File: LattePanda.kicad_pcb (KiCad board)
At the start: 2 copper layers, 70 x 88 mm, 18 parts, among them IC1 NJM2845MABDT

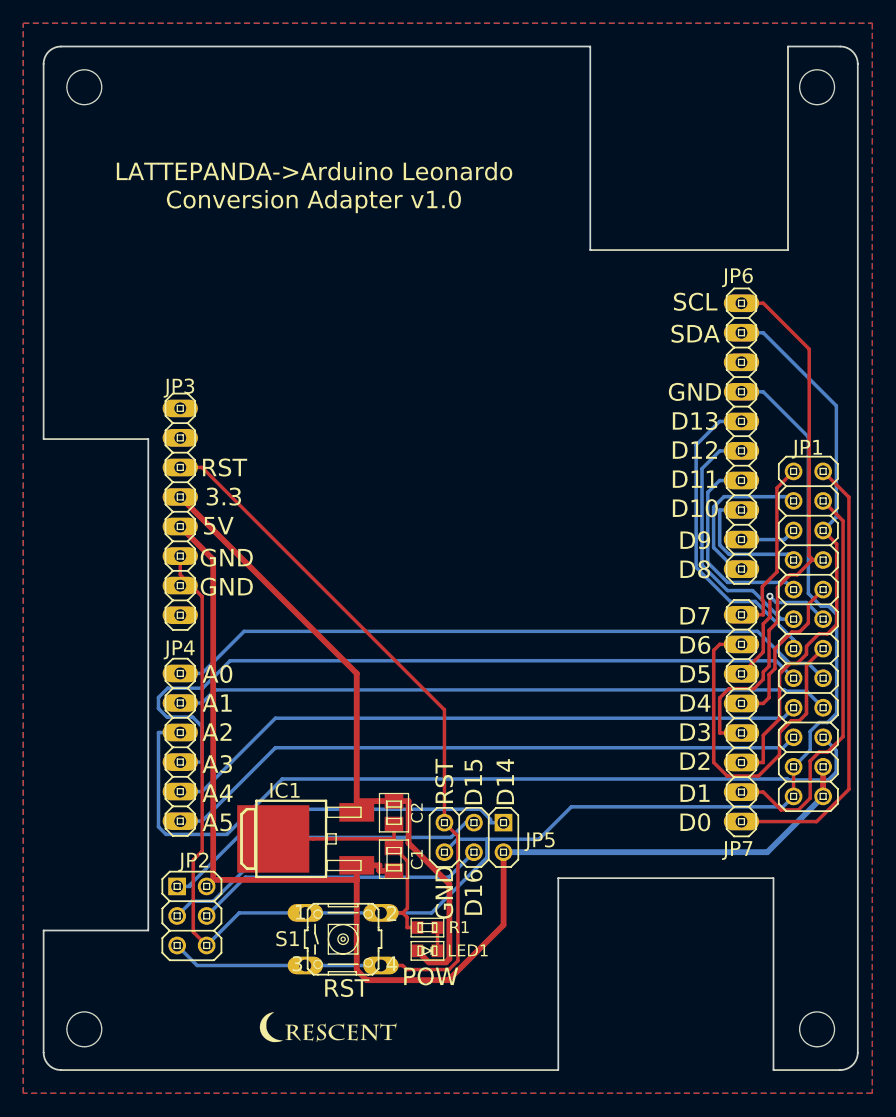
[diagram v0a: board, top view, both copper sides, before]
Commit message: Fixed the interference of LAN port.
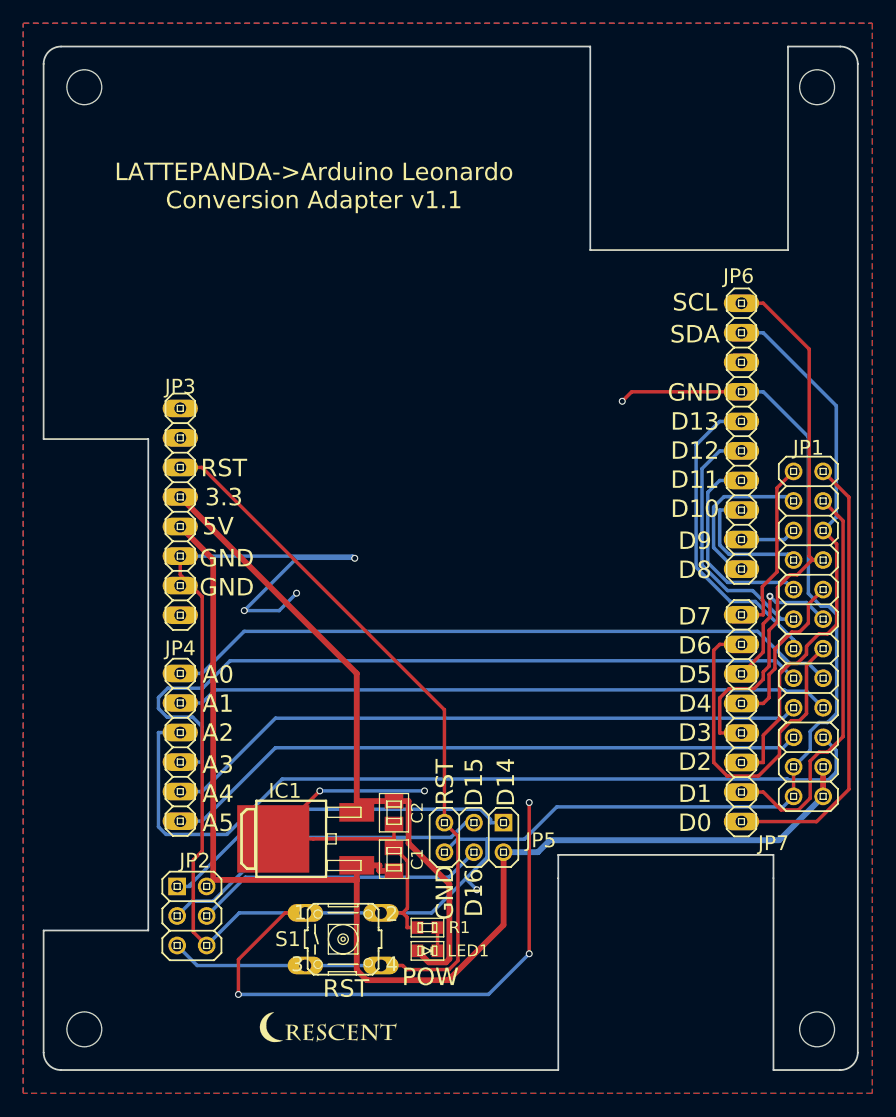
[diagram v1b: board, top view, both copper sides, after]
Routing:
- net GND: track 161.2 -> 269.3 mm, vias 0 -> 10
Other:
- outline, holes or cut-outs redrawn
- board text added: "LATTEPANDA->Arduino Leonardo Conversion Adapter v1.1"
- board text removed: "LATTEPANDA->Arduino Leonardo Conversion Adapter v1.0"
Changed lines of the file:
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@@
     (area 88.750001 44.65 181.740046 140.47626)
     (thickness 1.6)
-    (drawings 58)
-    (tracks 267)
+    (drawings 60)
+    (tracks 298)
     (zones 0)
     (modules 18)
@@
   (title_block
     (title "LattePanda to Arduino Leonard")
-    (date 2017-06-17)
-    (rev v1.0)
+    (date 2017-07-07)
+    (rev v1.1)
     (company Crescent)
   )
@@
     (tags "PIN HEADER")
     (attr virtual)
-    (fp_text reference JP7 (at -11.25 -0.25 180) (layer F.SilkS)
+    (fp_text reference JP7 (at -10.75 2.75 180) (layer F.SilkS)
       (effects (font (size 1.27 1.27) (thickness 0.127)))
     )
@@
       (net 2 GND))
   )
+  (gr_line (start 151 119.5) (end 151 121.5) (angle 90) (layer Edge.Cuts) (width 0.15))
+  (gr_line (start 169.5 119.5) (end 151 119.5) (angle 90) (layer Edge.Cuts) (width 0.15))
+  (gr_line (start 169.5 121.5) (end 169.5 119.5) (angle 90) (layer Edge.Cuts) (width 0.15))
   (gr_text POW (at 140 130) (layer F.SilkS)
     (effects (font (size 1.5 1.5) (thickness 0.3)))
@@
     (effects (font (size 1.5 1.5) (thickness 0.3)))
   )
-  (gr_text "LATTEPANDA->Arduino Leonardo\nConversion Adapter v1.0" (at 130 62) (layer F.SilkS)
+  (gr_text "LATTEPANDA->Arduino Leonardo\nConversion Adapter v1.1" (at 130 62) (layer F.SilkS)
     (effects (font (size 1.5 1.5) (thickness 0.3)))
   )
@@
   (gr_line (start 169.5 138) (end 175.25 138) (angle 90) (layer Edge.Cuts) (width 0.15))
   (gr_line (start 169.5 121.5) (end 169.5 138) (angle 90) (layer Edge.Cuts) (width 0.15))
-  (gr_line (start 151 121.5) (end 169.5 121.5) (angle 90) (layer Edge.Cuts) (width 0.15))
   (gr_line (start 151 138) (end 151 121.5) (angle 90) (layer Edge.Cuts) (width 0.15))
   (gr_line (start 108.25 138) (end 151 138) (angle 90) (layer Edge.Cuts) (width 0.15))
@@
     (arrow2b (pts (xy 110.25 47.5) (xy 111.376504 46.913579)))
   )
+  (segment (start 170 118.24) (end 150.28 118.24) (width 0.5) (layer B.Cu) (net 1))
+  (segment (start 173.77 114.47) (end 170 118.24) (width 0.5) (layer B.Cu) (net 1))
+  (segment (start 149.25 119.27) (end 146.29 119.27) (width 0.5) (layer B.Cu) (net 1))
+  (segment (start 150.28 118.24) (end 149.25 119.27) (width 0.5) (layer B.Cu) (net 1))
   (segment (start 135.6233 120.8706) (end 135.6259 120.8732) (width 0.5) (layer F.Cu) (net 1))
   (segment (start 135.6233 120.4034) (end 135.6233 120.8706) (width 0.5) (layer F.Cu) (net 1))
@@
   (segment (start 121.3275 121.6525) (end 120.77 122.21) (width 0.5) (layer F.Cu) (net 1))
   (segment (start 173.77 114.47) (end 173.77 111.93) (width 0.5) (layer F.Cu) (net 1))
-  (segment (start 168.97 119.27) (end 146.29 119.27) (width 0.5) (layer B.Cu) (net 1))
-  (segment (start 173.77 114.47) (end 168.97 119.27) (width 0.5) (layer B.Cu) (net 1))
   (segment (start 133.6731 121.6525) (end 121.3275 121.6525) (width 0.5) (layer F.Cu) (net 1))
   (segment (start 146.29 125.5301) (end 146.29 119.27) (width 0.5) (layer F.Cu) (net 1))
@@
   (segment (start 133.6731 129.4095) (end 134.5343 130.2707) (width 0.5) (layer F.Cu) (net 1))
   (segment (start 133.6731 121.6525) (end 133.6731 129.4095) (width 0.5) (layer F.Cu) (net 1))
+  (segment (start 148.5 115) (end 148.5 128) (width 0.3) (layer F.Cu) (net 2))
+  (segment (start 145 131.5) (end 148.5 128) (width 0.3) (layer B.Cu) (net 2))
+  (via (at 148.5 128) (size 0.6) (drill 0.4) (layers F.Cu B.Cu) (net 2))
+  (segment (start 127.5106 124.4894) (end 129.2488 124.4894) (width 0.3) (layer F.Cu) (net 2))
+  (via (at 123.5 131.5) (size 0.6) (drill 0.4) (layers F.Cu B.Cu) (net 2))
+  (segment (start 123.5 128.5) (end 123.5 131.5) (width 0.3) (layer F.Cu) (net 2))
+  (segment (start 127.5106 124.4894) (end 123.5 128.5) (width 0.3) (layer F.Cu) (net 2))
+  (segment (start 123.5 131.5) (end 145 131.5) (width 0.3) (layer B.Cu) (net 2))
+  (via (at 148.5 115) (size 0.6) (drill 0.4) (layers F.Cu B.Cu) (net 2))
+  (segment (start 143.04745 121.54745) (end 144 122.5) (width 0.3) (layer B.Cu) (net 2))
+  (via (at 144 122.5) (size 0.6) (drill 0.4) (layers F.Cu B.Cu) (net 2))
+  (segment (start 124 98.5) (end 127 98.5) (width 0.3) (layer B.Cu) (net 2))
+  (segment (start 128.5 94) (end 124 98.5) (width 0.3) (layer B.Cu) (net 2))
+  (via (at 124 98.5) (size 0.6) (drill 0.4) (layers F.Cu B.Cu) (net 2))
+  (segment (start 118.5 93.81) (end 133.31 93.81) (width 0.3) (layer B.Cu) (net 2))
+  (via (at 133.5 94) (size 0.6) (drill 0.4) (layers F.Cu B.Cu) (net 2))
+  (segment (start 133.31 93.81) (end 133.5 94) (width 0.3) (layer B.Cu) (net 2))
+  (segment (start 133.5 94) (end 128.5 94) (width 0.3) (layer B.Cu) (net 2))
+  (via (at 128.5 97) (size 0.6) (drill 0.4) (layers F.Cu B.Cu) (net 2))
+  (segment (start 127 98.5) (end 128.5 97) (width 0.3) (layer B.Cu) (net 2))
+  (segment (start 139.5 114) (end 130.5 114) (width 0.3) (layer B.Cu) (net 2))
+  (via (at 130.5 114) (size 0.6) (drill 0.4) (layers F.Cu B.Cu) (net 2))
+  (segment (start 130.5 114) (end 126.49502 118.00498) (width 0.3) (layer F.Cu) (net 2))
+  (via (at 139.5 114) (size 0.6) (drill 0.4) (layers F.Cu B.Cu) (net 2))
+  (segment (start 126.49502 118.125) (end 126.49502 118.00498) (width 0.3) (layer F.Cu) (net 2))
+  (segment (start 166.75 79.69) (end 157.31 79.69) (width 0.3) (layer F.Cu) (net 2))
+  (via (at 156.5 80.5) (size 0.6) (drill 0.4) (layers F.Cu B.Cu) (net 2))
+  (segment (start 157.31 79.69) (end 156.5 80.5) (width 0.3) (layer F.Cu) (net 2))
   (segment (start 171.23 114.47) (end 171.23 111.93) (width 0.3) (layer F.Cu) (net 2))
   (segment (start 123.5706 124.4894) (end 120.77 127.29) (width 0.3) (layer B.Cu) (net 2))
@@
   (segment (start 138.0242 120.026) (end 138.0242 124.0907) (width 0.3) (layer F.Cu) (net 2))
   (segment (start 136.875 118.8768) (end 138.0242 120.026) (width 0.3) (layer F.Cu) (net 2))
-  (segment (start 149.341 118.1538) (end 144.8722 118.1538) (width 0.3) (layer B.Cu) (net 2))
-  (segment (start 152.1248 115.37) (end 149.341 118.1538) (width 0.3) (layer B.Cu) (net 2))
-  (segment (start 170.33 115.37) (end 152.1248 115.37) (width 0.3) (layer B.Cu) (net 2))
+  (segment (start 148.091 118.1538) (end 144.8722 118.1538) (width 0.3) (layer B.Cu) (net 2))
+  (segment (start 150.8748 115.37) (end 148.091 118.1538) (width 0.3) (layer B.Cu) (net 2))
+  (segment (start 170.33 115.37) (end 150.8748 115.37) (width 0.3) (layer B.Cu) (net 2))
   (segment (start 171.23 114.47) (end 170.33 115.37) (width 0.3) (layer B.Cu) (net 2))
   (segment (start 142.3262 118.1538) (end 141.21 119.27) (width 0.3) (layer B.Cu) (net 2))
@@
   (segment (start 129.2488 124.4894) (end 135.7512 124.4894) (width 0.3) (layer B.Cu) (net 2))
   (segment (start 144.8722 119.7227) (end 144.8722 118.1538) (width 0.3) (layer B.Cu) (net 2))
-  (segment (start 140.1055 124.4894) (end 144.8722 119.7227) (width 0.3) (layer B.Cu) (net 2))
+  (segment (start 140.1055 124.4894) (end 143.04745 121.54745) (width 0.3) (layer B.Cu) (net 2))
+  (segment (start 143.04745 121.54745) (end 144.8722 119.7227) (width 0.3) (layer B.Cu) (net 2))
   (segment (start 135.7512 124.4894) (end 140.1055 124.4894) (width 0.3) (layer B.Cu) (net 2))
   (segment (start 172.5 83.5657) (end 168.6243 79.69) (width 0.3) (layer B.Cu) (net 2))
